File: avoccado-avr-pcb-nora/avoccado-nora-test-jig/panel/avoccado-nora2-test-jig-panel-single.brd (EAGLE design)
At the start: 25 x 25 mm, 24 parts

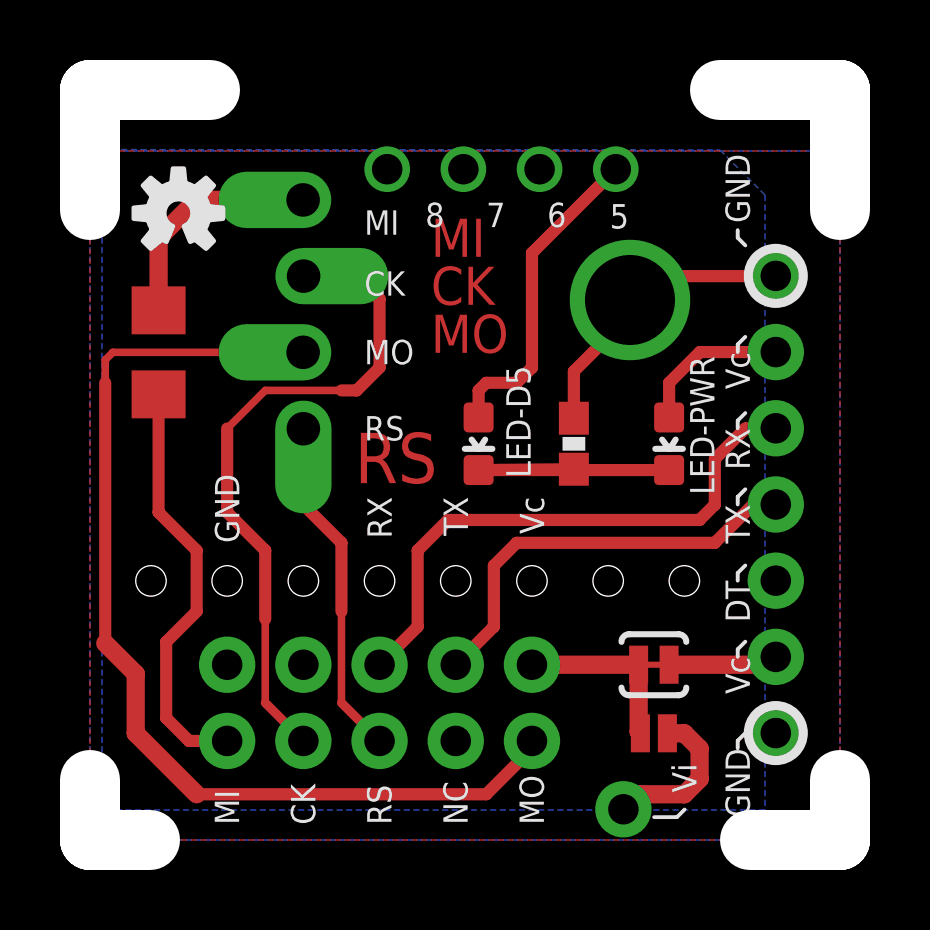
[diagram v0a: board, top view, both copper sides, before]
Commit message: test alignment of test jig panel
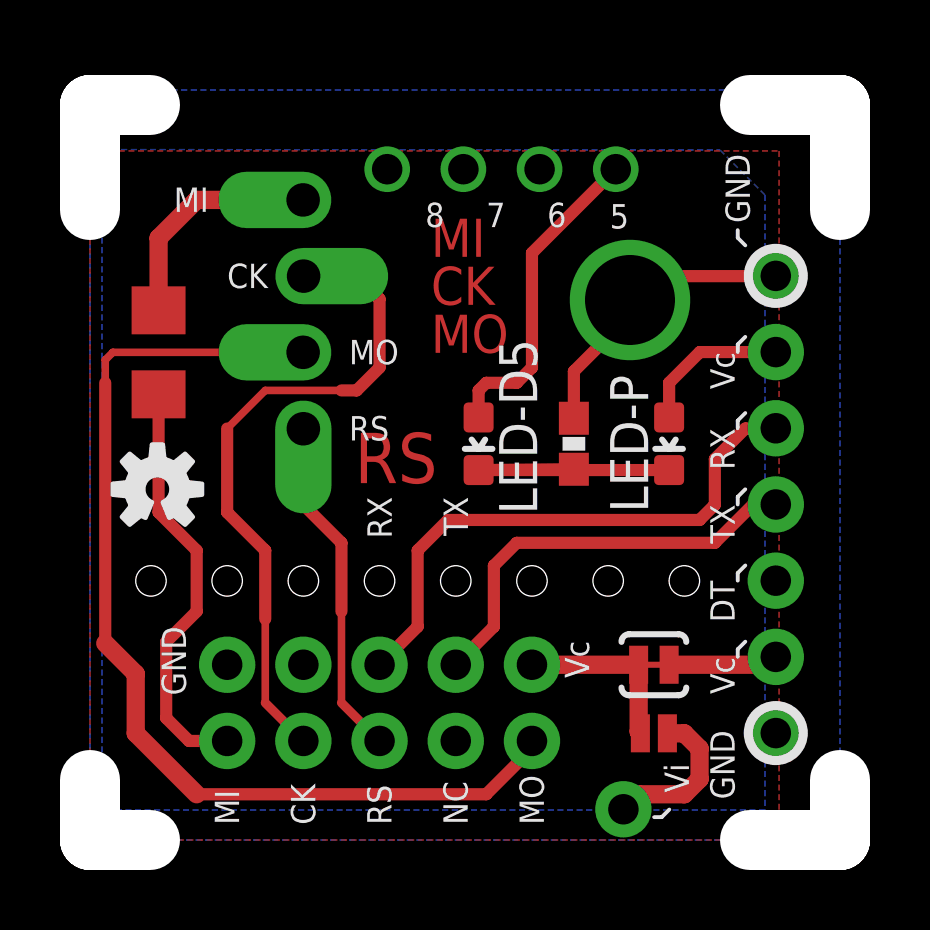
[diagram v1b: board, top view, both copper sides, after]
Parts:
- moved LOGO2 9.23 mm to (2.25, 11.7)
- renumbered LED-D5 to D5-LED, LED-PWR to PWR-LED
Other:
- board size 25 x 25 mm -> 25 x 24.5 mm
- board text added: "LED-D5"
- board text added: "LED-P"
